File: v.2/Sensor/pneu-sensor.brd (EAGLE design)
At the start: 30.5 x 50.8 mm, 18 parts, among them U1 V_REG_LD1117V5, U2 ADS1015

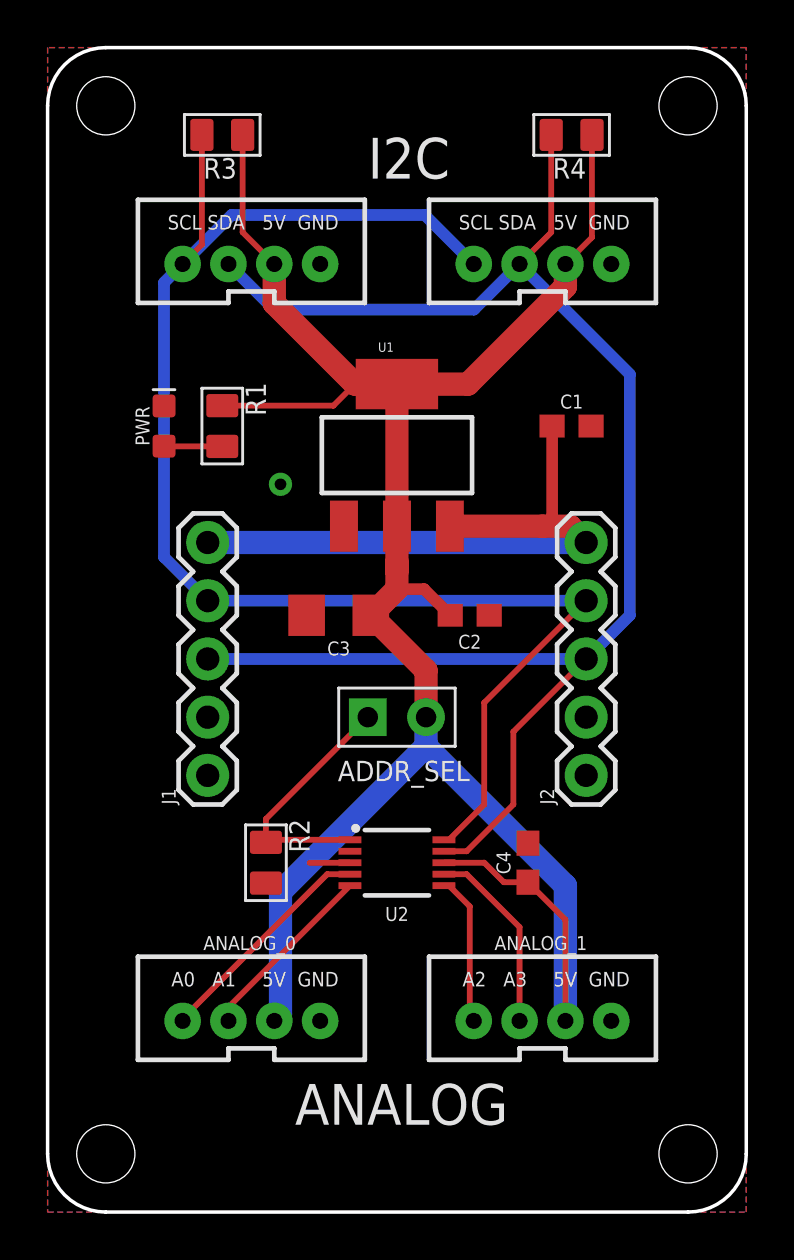
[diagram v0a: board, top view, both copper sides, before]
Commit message: updated sensor board
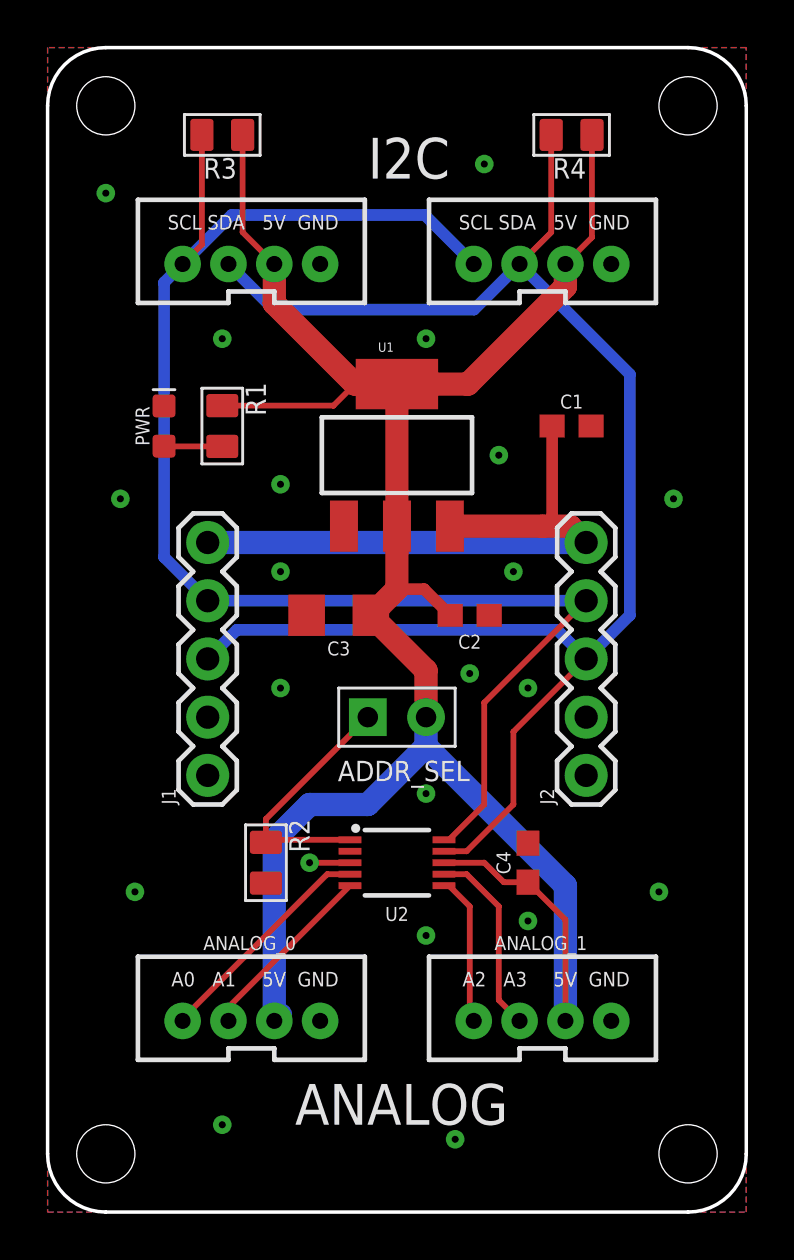
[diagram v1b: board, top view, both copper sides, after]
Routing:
- net +5V: track 97.6 -> 99.0 mm
- net SDA: track 68.6 -> 69.7 mm
- net GND: vias 1 -> 21
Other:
- board text added: "08/07/2018"
- board text added: "Byron Xu"
- board text added: "Jifei Ou"

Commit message: modified sensor board
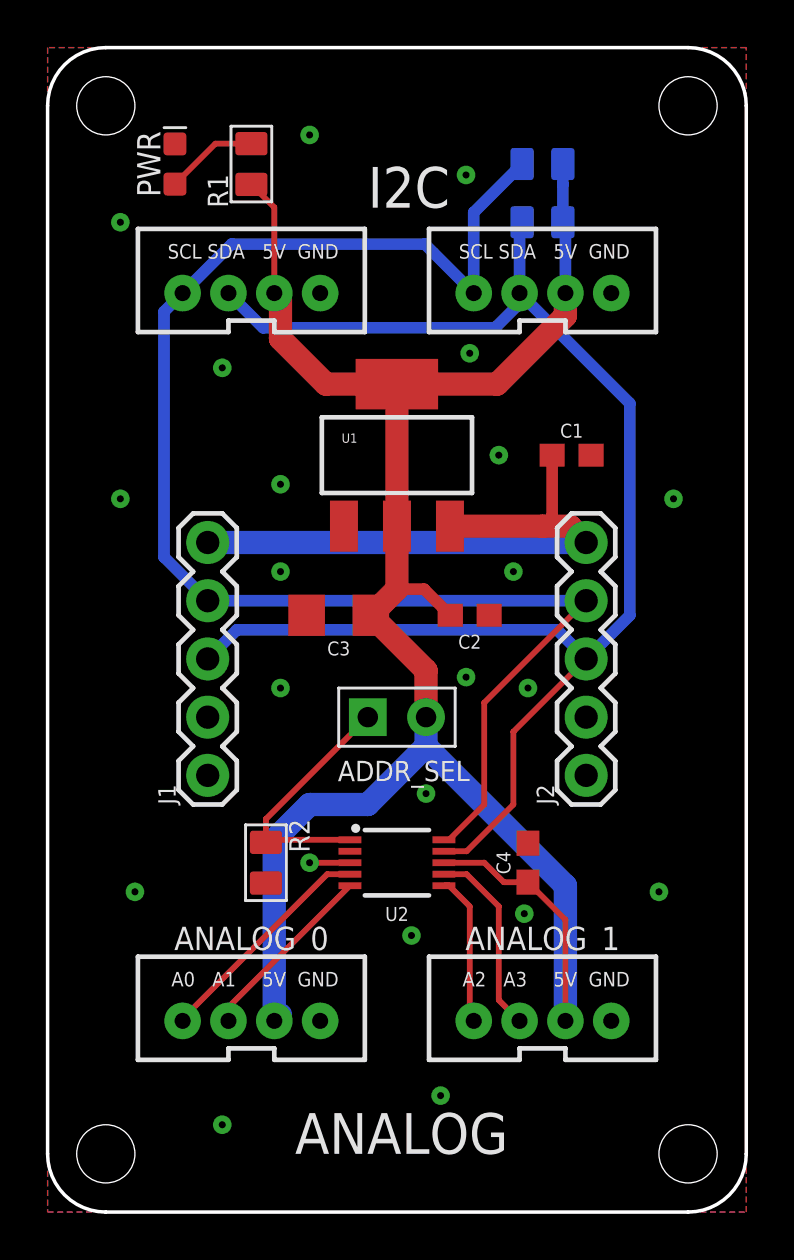
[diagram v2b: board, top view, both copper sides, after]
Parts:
- moved R3 14.0 mm to (19.1, 45.7), flipped to the bottom, turned to 90 degrees
- moved R1 11.5 mm to (6.35, 45.7), turned to 180 degrees
- moved PWR 11.4 mm to (3.02, 45.7)
- moved R4 4.02 mm to (19.1, 43.2), flipped to the bottom, turned to 90 degrees
- moved C1 1.27 mm to (20.3, 33.0)
- moved I2C_0 1.27 mm to (6.35, 40.6)
- moved I2C_1 1.27 mm to (19.1, 40.6)
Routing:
- net +5V: track 99.0 -> 90.3 mm
- net SDA: track 69.7 -> 65.2 mm
- net N$3: track 2.54 -> 4.07 mm
- net 12V: track 27.3 -> 26.0 mm
- net SCL: track 65.9 -> 65.2 mm
- net GND: vias 21 -> 22
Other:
- board text added: "08/16/2018"
- board text removed: "08/07/2018"
